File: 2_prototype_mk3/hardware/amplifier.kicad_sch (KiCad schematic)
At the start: 8 parts, among them U5 MAX98357A

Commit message: MKIII design refinements
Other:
- title: (none) -> Amplifier
- moved on the sheet: C1, C2, C5, C6, FB1, FB2, H6, U5

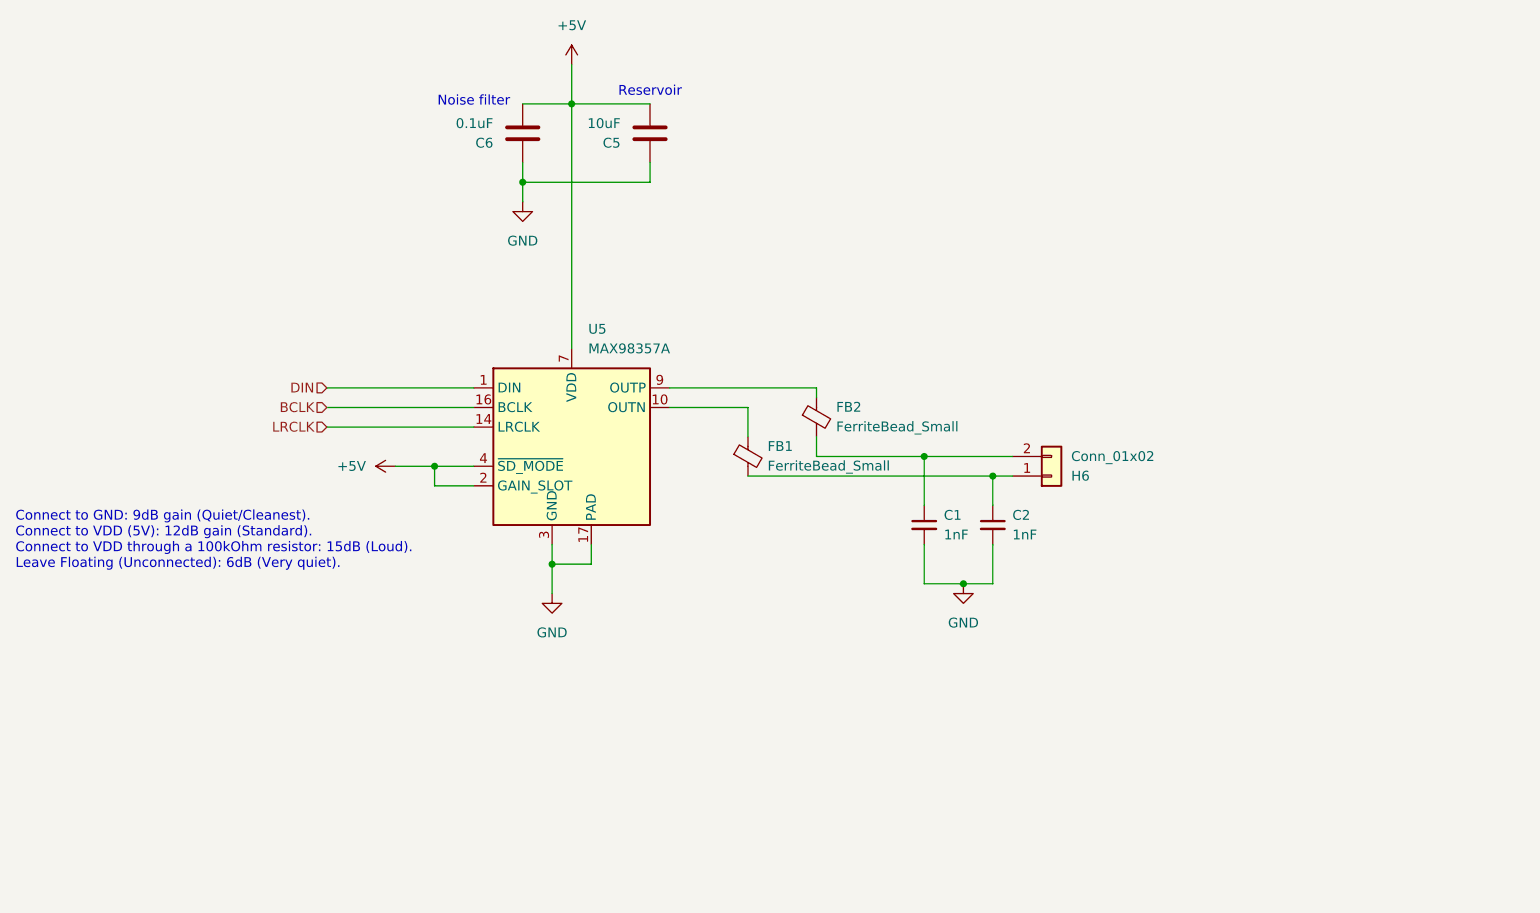
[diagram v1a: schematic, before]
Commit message: Add net classes for power
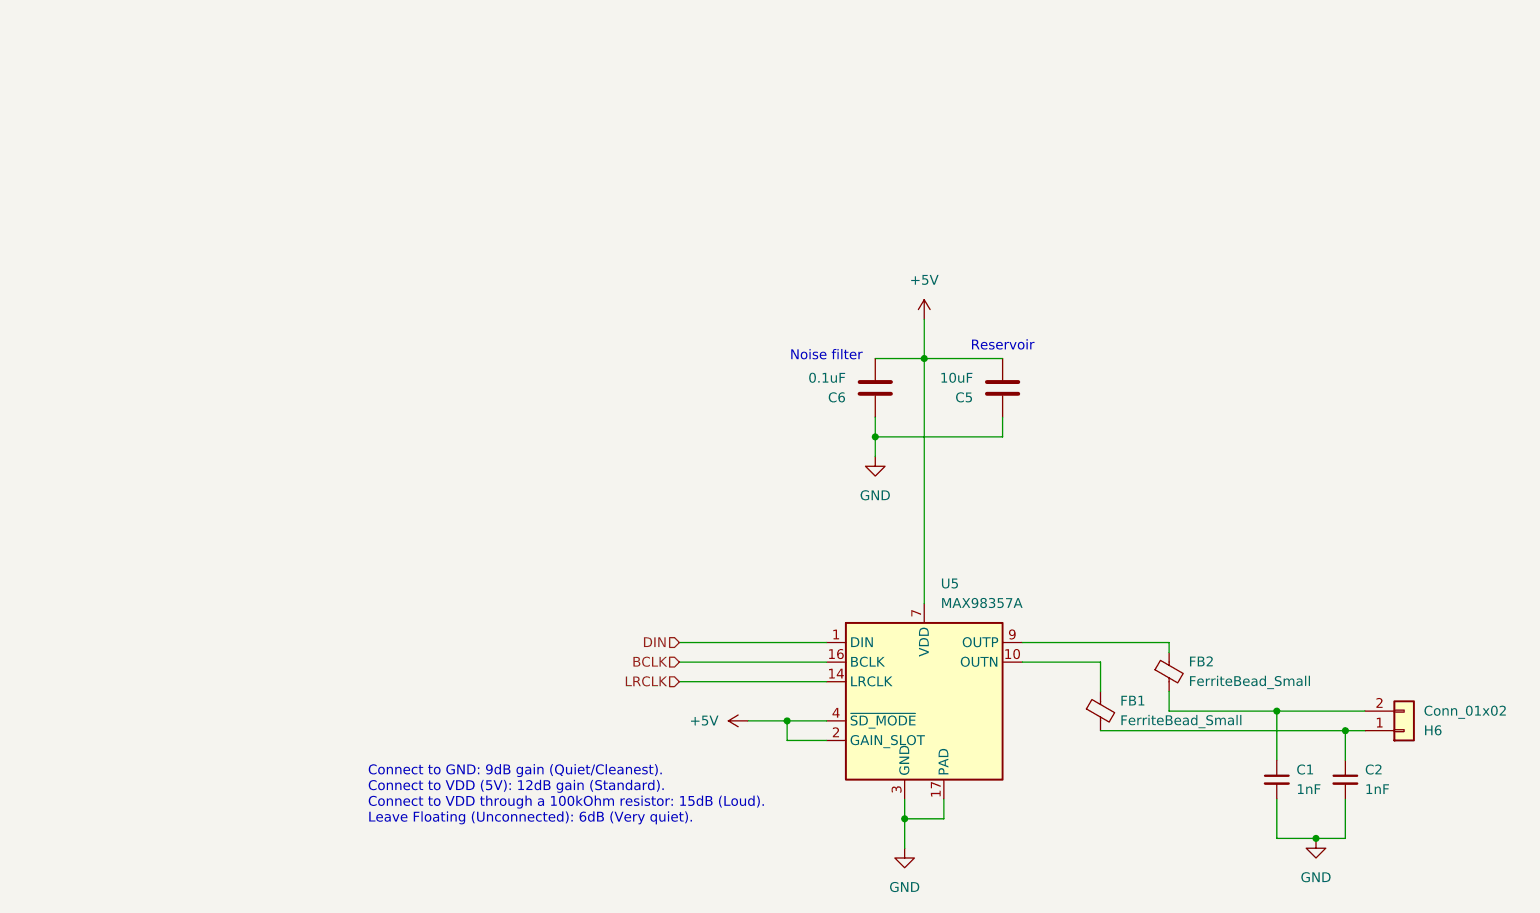
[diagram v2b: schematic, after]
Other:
- title: Amplifier -> (none)
- moved on the sheet: C1, C2, C5, C6, FB1, FB2, H6, U5

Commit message: MKIII PCB components connected and passing DRC
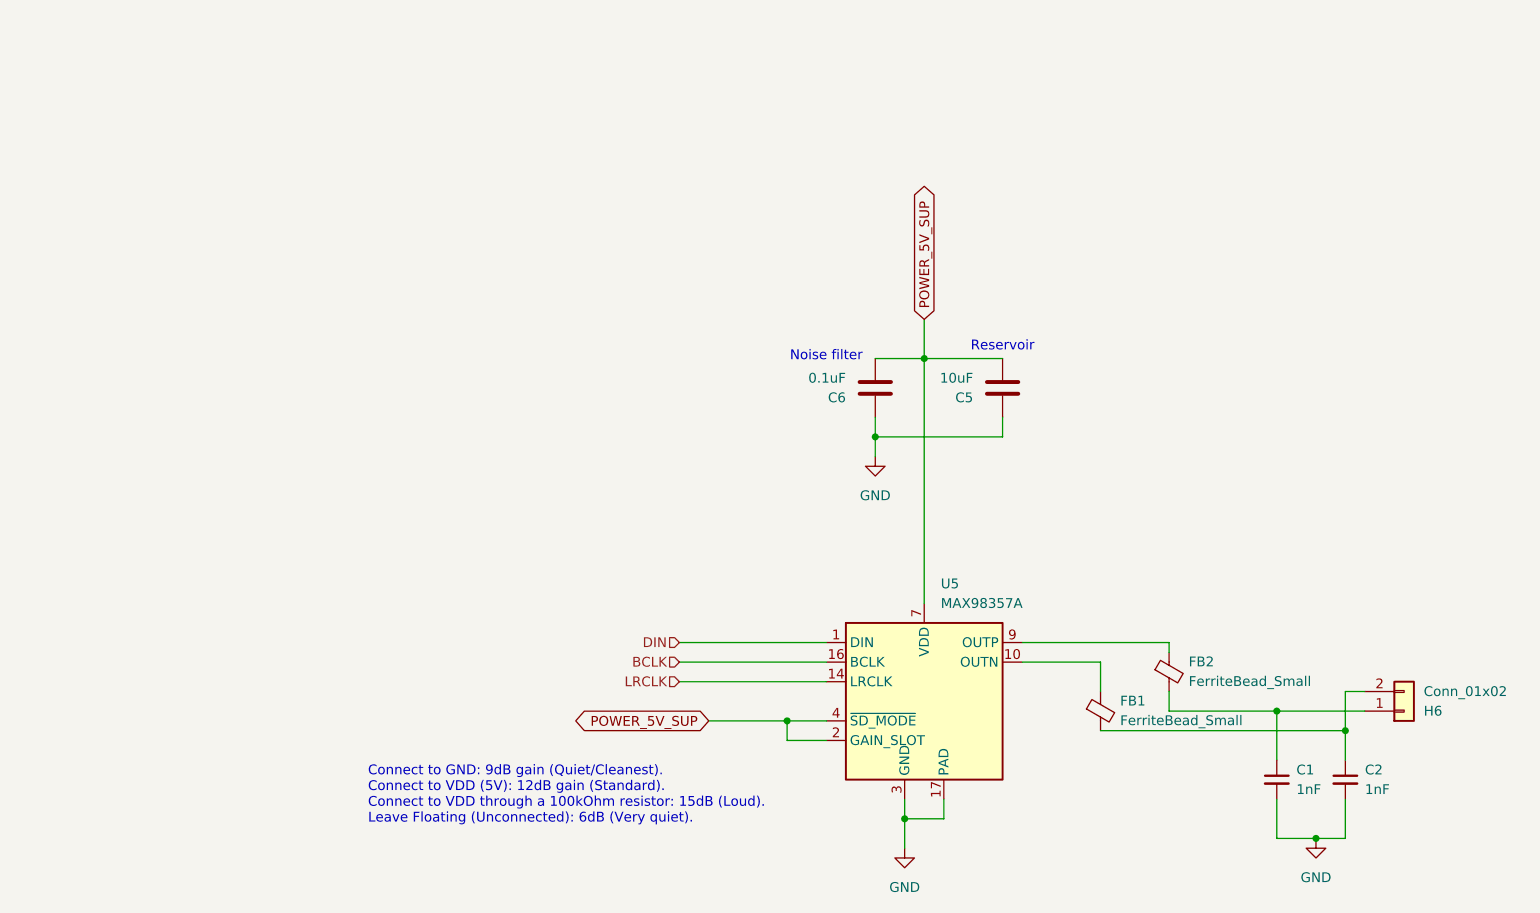
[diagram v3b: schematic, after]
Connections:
- net at C1.1, FB2.2: now also H6.1 (Pin_1); no longer H6.2 (Pin_2)
- net at C2.1, FB1.2: now also H6.2 (Pin_2); no longer H6.1 (Pin_1)
- net +5V renamed POWER_5V_SUP
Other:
- moved on the sheet: H6
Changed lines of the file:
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@@
+	)
+	(junction
+		(at 195.58 106.68)
+		(diameter 0)
+		(color 0 0 0 0)
 	)
 	(junction
@@
 		(color 0 0 0 0)
 	)
-	(junction
-		(at 195.58 106.68)
-		(diameter 0)
-		(color 0 0 0 0)
-	)
 	(wire
 		(pts
@@
 	(wire
 		(pts
-			(xy 204.47 109.22) (xy 207.01 109.22)
-		)
-		(stroke
-			(width 0)
-			(type default)
-		)
-	)
-	(wire
-		(pts
-			(xy 127 107.95) (xy 132.08 107.95)
-		)
-		(stroke
-			(width 0)
-			(type default)
-		)
-	)
-	(wire
-		(pts
 			(xy 195.58 106.68) (xy 195.58 113.03)
 		)
@@
 	(wire
 		(pts
+			(xy 204.47 109.22) (xy 204.47 104.14)
+		)
+		(stroke
+			(width 0)
+			(type default)
+		)
+	)
+	(wire
+		(pts
 			(xy 162.56 97.79) (xy 181.61 97.79)
 		)
@@
 	(wire
 		(pts
+			(xy 204.47 104.14) (xy 207.01 104.14)
+		)
+		(stroke
+			(width 0)
+			(type default)
+		)
+	)
+	(wire
+		(pts
 			(xy 143.51 71.12) (xy 143.51 73.66)
 		)
@@
 	(wire
 		(pts
+			(xy 181.61 106.68) (xy 195.58 106.68)
+		)
+		(stroke
+			(width 0)
+			(type default)
+		)
+	)
+	(wire
+		(pts
+			(xy 195.58 123.19) (xy 200.66 123.19)
+		)
+		(stroke
+			(width 0)
+			(type default)
+		)
+	)
+	(wire
+		(pts
+			(xy 143.51 60.96) (xy 149.86 60.96)
+		)
+		(stroke
+			(width 0)
+			(type default)
+		)
+	)
+	(wire
+		(pts
 			(xy 195.58 106.68) (xy 207.01 106.68)
 		)
@@
 	(wire
 		(pts
-			(xy 181.61 106.68) (xy 195.58 106.68)
-		)
-		(stroke
-			(width 0)
-			(type default)
-		)
-	)
-	(wire
-		(pts
-			(xy 195.58 123.19) (xy 200.66 123.19)
-		)
-		(stroke
-			(width 0)
-			(type default)
-		)
-	)
-	(wire
-		(pts
-			(xy 143.51 60.96) (xy 149.86 60.96)
-		)
-		(stroke
-			(width 0)
-			(type default)
-		)
-	)
-	(wire
-		(pts
 			(xy 181.61 104.14) (xy 181.61 106.68)
 		)
@@
 	(wire
 		(pts
+			(xy 121.92 107.95) (xy 132.08 107.95)
+		)
+		(stroke
+			(width 0)
+			(type default)
+		)
+	)
+	(wire
+		(pts
 			(xy 195.58 118.11) (xy 195.58 123.19)
 		)
@@
 			(width 0)
 			(type default)
+		)
+	)
+	(global_label "POWER_5V_SUP"
+		(shape bidirectional)
+		(at 149.86 55.88 90)
+		(fields_autoplaced yes)
+		(effects
+			(font
+				(size 1.27 1.27)
+			)
+			(justify left)
+		)
+		(property "Intersheetrefs" "${INTERSHEET_REFS}"
+			(at 149.86 37.2693 90)
+			(effects
+				(font
+					(size 1.27 1.27)
+				)
+				(justify left)
+				(hide yes)
+			)
+		)
+	)
+	(global_label "POWER_5V_SUP"
+		(shape bidirectional)
+		(at 121.92 107.95 180)
+		(fields_autoplaced yes)
+		(effects
+			(font
+				(size 1.27 1.27)
+			)
+			(justify right)
+		)
+		(property "Intersheetrefs" "${INTERSHEET_REFS}"
+			(at 103.3093 107.95 0)
+			(effects
+				(font
+					(size 1.27 1.27)
+				)
+				(justify right)
+				(hide yes)
+			)
 		)
 	)
@@
 			(justify left bottom)
 		)
-		(property "Netclass" "POWER_5v"
+		(property "Netclass" "POWER_5V_SUP"
 			(at 127.6985 105.41 0)
 			(effects
@@
 			(justify left bottom)
 		)
-		(property "Netclass" "POWER_5v"
+		(property "Netclass" "POWER_5V_SUP"
 			(at 147.32 57.7215 90)
 			(effects
@@
 	(symbol
 		(lib_id "Connector_Generic:Conn_01x02")
-		(at 212.09 109.22 0)
+		(at 212.09 106.68 0)
 		(mirror x)
 		(unit 1)
@@
 		(dnp no)
 		(property "Reference" "H6"
-			(at 214.63 109.2201 0)
+			(at 214.63 106.6801 0)
 			(effects
 				(font
@@
 		)
 		(property "Value" "Conn_01x02"
-			(at 214.63 106.6801 0)
+			(at 214.63 104.1401 0)
 			(effects
 				(font
@@
 		)
 		(property "Footprint" "TerminalBlock_Phoenix:TerminalBlock_Phoenix_PT-1,5-2-3.5-H_1x02_P3.50mm_Horizontal"
-			(at 212.09 109.22 0)
+			(at 212.09 106.68 0)
 			(effects
 				(font
@@
 		)
 		(property "Datasheet" "~"
-			(at 212.09 109.22 0)
+			(at 212.09 106.68 0)
 			(effects
 				(font
@@
 		)
 		(property "Description" "Generic connector, single row, 01x02, script generated (kicad-library-utils/schlib/autogen/connector/)"
-			(at 212.09 109.22 0)
+			(at 212.09 106.68 0)
 			(effects
 				(font
@@
 	)
 	(symbol
-		(lib_id "power:+5V")
-		(at 149.86 55.88 0)
-		(unit 1)
-		(exclude_from_sim no)
-		(in_bom yes)
-		(on_board yes)
-		(dnp no)
-		(fields_autoplaced yes)
-		(property "Reference" "#PWR029"
-			(at 149.86 59.69 0)
-			(effects
-				(font
-					(size 1.27 1.27)
-				)
-				(hide yes)
-			)
-		)
-		(property "Value" "+5V"
-			(at 149.86 50.8 0)
-			(effects
-				(font
-					(size 1.27 1.27)
-				)
-			)
-		)
-		(property "Footprint" ""
-			(at 149.86 55.88 0)
-			(effects
-				(font
-					(size 1.27 1.27)
-				)
-				(hide yes)
-			)
-		)
-		(property "Datasheet" ""
-			(at 149.86 55.88 0)
-			(effects
-				(font
-					(size 1.27 1.27)
-				)
-				(hide yes)
-			)
-		)
-		(property "Description" "Power symbol creates a global label with name \"+5V\""
-			(at 149.86 55.88 0)
-			(effects
-				(font
-					(size 1.27 1.27)
-				)
-				(hide yes)
-			)
-		)
-		(pin "1"
-		)
-		(instances
-			(project ""
-				(path "/5a2f0aa7-670f-4d0d-8d56-ad98c847383a/a3500c8b-1cb4-4280-8b2f-37934c522aa7"
-					(reference "#PWR029")
-					(unit 1)
-				)
-			)
-		)
-	)
-	(symbol
 		(lib_id "Audio:MAX98357A")
 		(at 149.86 105.41 0)
@@
 					(unit 1)
 				)
-			)
-		)
-	)
-	(symbol
-		(lib_id "power:+5V")
-		(at 127 107.95 90)
-		(unit 1)
-		(exclude_from_sim no)
-		(in_bom yes)
-		(on_board yes)
-		(dnp no)
-		(fields_autoplaced yes)
-		(property "Reference" "#PWR016"
-			(at 130.81 107.95 0)
-			(effects
-				(font
-					(size 1.27 1.27)
-				)
-				(hide yes)
-			)
-		)
-		(property "Value" "+5V"
-			(at 123.19 107.9499 90)
-			(effects
-				(font
-					(size 1.27 1.27)
-				)
-				(justify left)
-			)
-		)
-		(property "Footprint" ""
-			(at 127 107.95 0)
-			(effects
-				(font
-					(size 1.27 1.27)
-				)
-				(hide yes)
-			)
-		)
-		(property "Datasheet" ""
-			(at 127 107.95 0)
-			(effects
-				(font
-					(size 1.27 1.27)
-				)
-				(hide yes)
-			)
-		)
-		(property "Description" "Power symbol creates a global label with name \"+5V\""
-			(at 127 107.95 0)
-			(effects
-				(font
-					(size 1.27 1.27)
-				)
-				(hide yes)
-			)
-		)
-		(pin "1"
-		)
-		(instances
-			(project ""
-				(path "/5a2f0aa7-670f-4d0d-8d56-ad98c847383a/a3500c8b-1cb4-4280-8b2f-37934c522aa7"
-					(reference "#PWR016")
-					(unit 1)
-				)

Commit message: Add manufacturer part nu bers
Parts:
- C1, C2: Manufacturer_Part_Number (none) -> 0603B102K500NT
- C5: Manufacturer_Part_Number (none) -> CL31A106KAHNNNE
- C6: Manufacturer_Part_Number (none) -> CL10B104KO8NNNC
- FB1, FB2: Manufacturer_Part_Number (none) -> BLM21PG221SN1D
- U5: Manufacturer_Part_Number (none) -> MAX98357AETE+T
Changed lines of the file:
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@@
+			)
+		)
+		(property "Manufacturer_Part_Number" "0603B102K500NT"
+			(at 195.58 115.57 0)
+			(effects
+				(font
+					(size 1.27 1.27)
+				)
+				(hide yes)
 			)
 		)
@@
 			)
 		)
+		(property "Manufacturer_Part_Number" ""
+			(at 212.09 106.68 0)
+			(effects
+				(font
+					(size 1.27 1.27)
+				)
+				(hide yes)
+			)
+		)
 		(pin "1"
 		)
@@
 			)
 		)
+		(property "Manufacturer_Part_Number" "CL10B104KO8NNNC"
+			(at 143.51 64.77 0)
+			(effects
+				(font
+					(size 1.27 1.27)
+				)
+				(hide yes)
+			)
+		)
 		(pin "2"
 		)
@@
 		)
 		(property "Description" "Unpolarized capacitor"
+			(at 160.02 64.77 0)
+			(effects
+				(font
+					(size 1.27 1.27)
+				)
+				(hide yes)
+			)
+		)
+		(property "Manufacturer_Part_Number" "CL31A106KAHNNNE"
 			(at 160.02 64.77 0)
 			(effects
@@
 			)
 		)
+		(property "Manufacturer_Part_Number" "MAX98357AETE+T"
+			(at 149.86 105.41 0)
+			(effects
+				(font
+					(size 1.27 1.27)
+				)
+				(hide yes)
+			)
+		)
 		(pin "16"
 		)
@@
 			)
 		)
+		(property "Manufacturer_Part_Number" "BLM21PG221SN1D"
+			(at 181.61 101.6 0)
+			(effects
+				(font
+					(size 1.27 1.27)
+				)
+				(hide yes)
+			)
+		)
 		(pin "1"
 		)
@@
 			)
 		)
+		(property "Manufacturer_Part_Number" "0603B102K500NT"
+			(at 204.47 115.57 0)
+			(effects
+				(font
+					(size 1.27 1.27)
+				)
+				(hide yes)
+			)
+		)
 		(pin "1"
 		)
@@
 			(at 172.72 106.68 0)
 			(effects
+				(font
+					(size 1.27 1.27)
+				)
+				(hide yes)
+			)
+		)
+		(property "Manufacturer_Part_Number" "BLM21PG221SN1D"
+			(at 172.72 106.68 0)
+			(effects
